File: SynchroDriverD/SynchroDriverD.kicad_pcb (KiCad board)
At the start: 2 copper layers, 100 x 100 mm, 201 parts, among them J1 SYNC, J2 POWER, J3 ROLL, J4 PITCH, J5 YAW, J6 NEEDLES, J7 FLAG, Q1 SIS990, Q2 SIS990, Q3 SIS990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

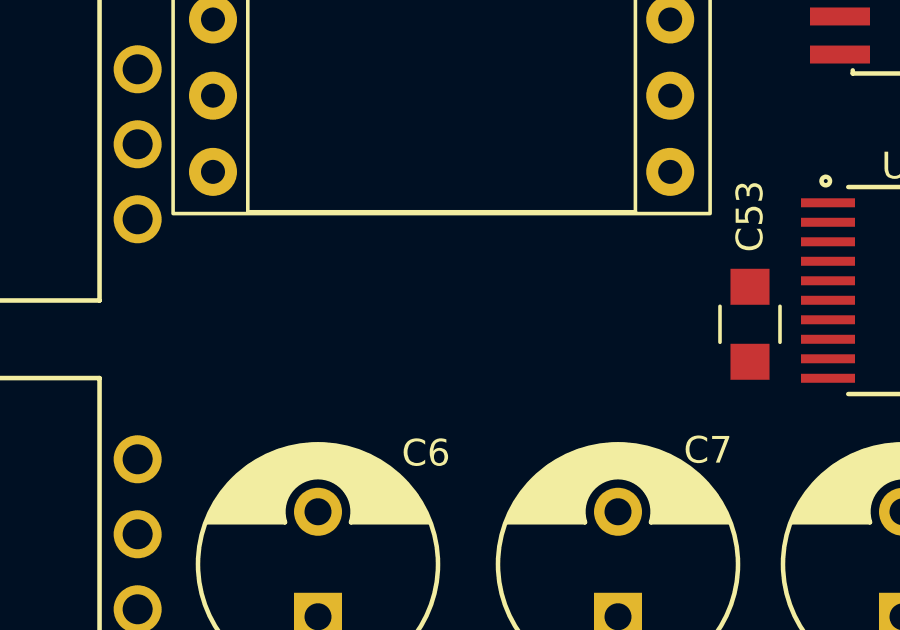
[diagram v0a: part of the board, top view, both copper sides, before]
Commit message: Ad flag drive circuit
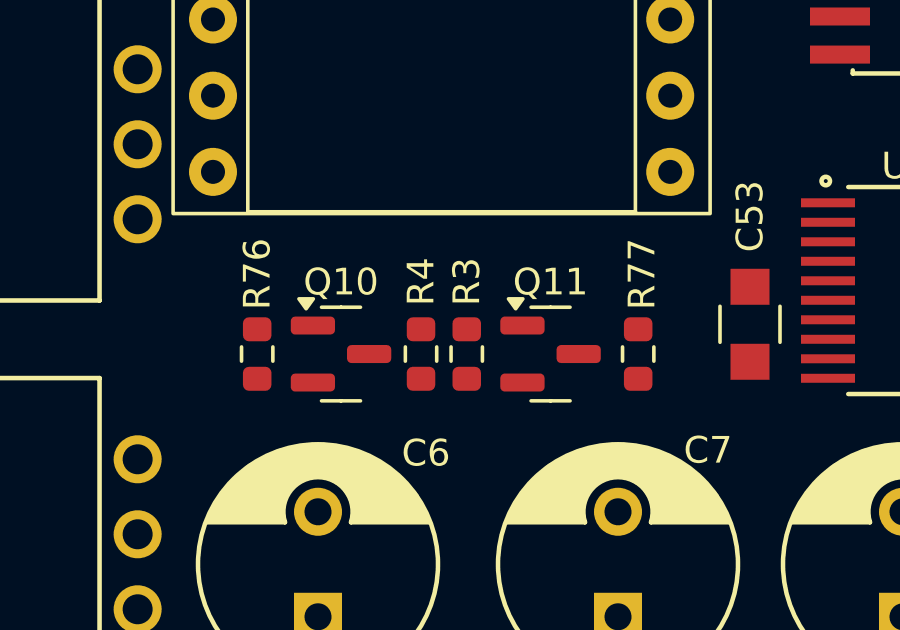
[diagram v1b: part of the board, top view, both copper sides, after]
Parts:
- added Q10: MMBTA42, Package_TO_SOT_SMD:SOT-23, F.Cu at (104.3, 126.5)
- added Q11: MMBTA92, Package_TO_SOT_SMD:SOT-23, F.Cu at (111.3, 126.5)
- added R3: 10K, Resistor_SMD:R_0603_1608Metric, F.Cu at (108.5, 126.5)
- added R4: 22K, Resistor_SMD:R_0603_1608Metric, F.Cu at (106.9, 126.5)
- added R76: 10K, Resistor_SMD:R_0603_1608Metric, F.Cu at (101.5, 126.5)
- added R77: 2.2K, Resistor_SMD:R_0603_1608Metric, F.Cu at (114.2, 126.5)
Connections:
- J7 pad 2: unconnected-(J7-Pin_2-Pad2) -> /FlagDriver/OUT
- U1 pad 18: unconnected-(U1-GP26-Pad18) -> /FLAG
